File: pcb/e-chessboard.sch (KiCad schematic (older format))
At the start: 46 parts

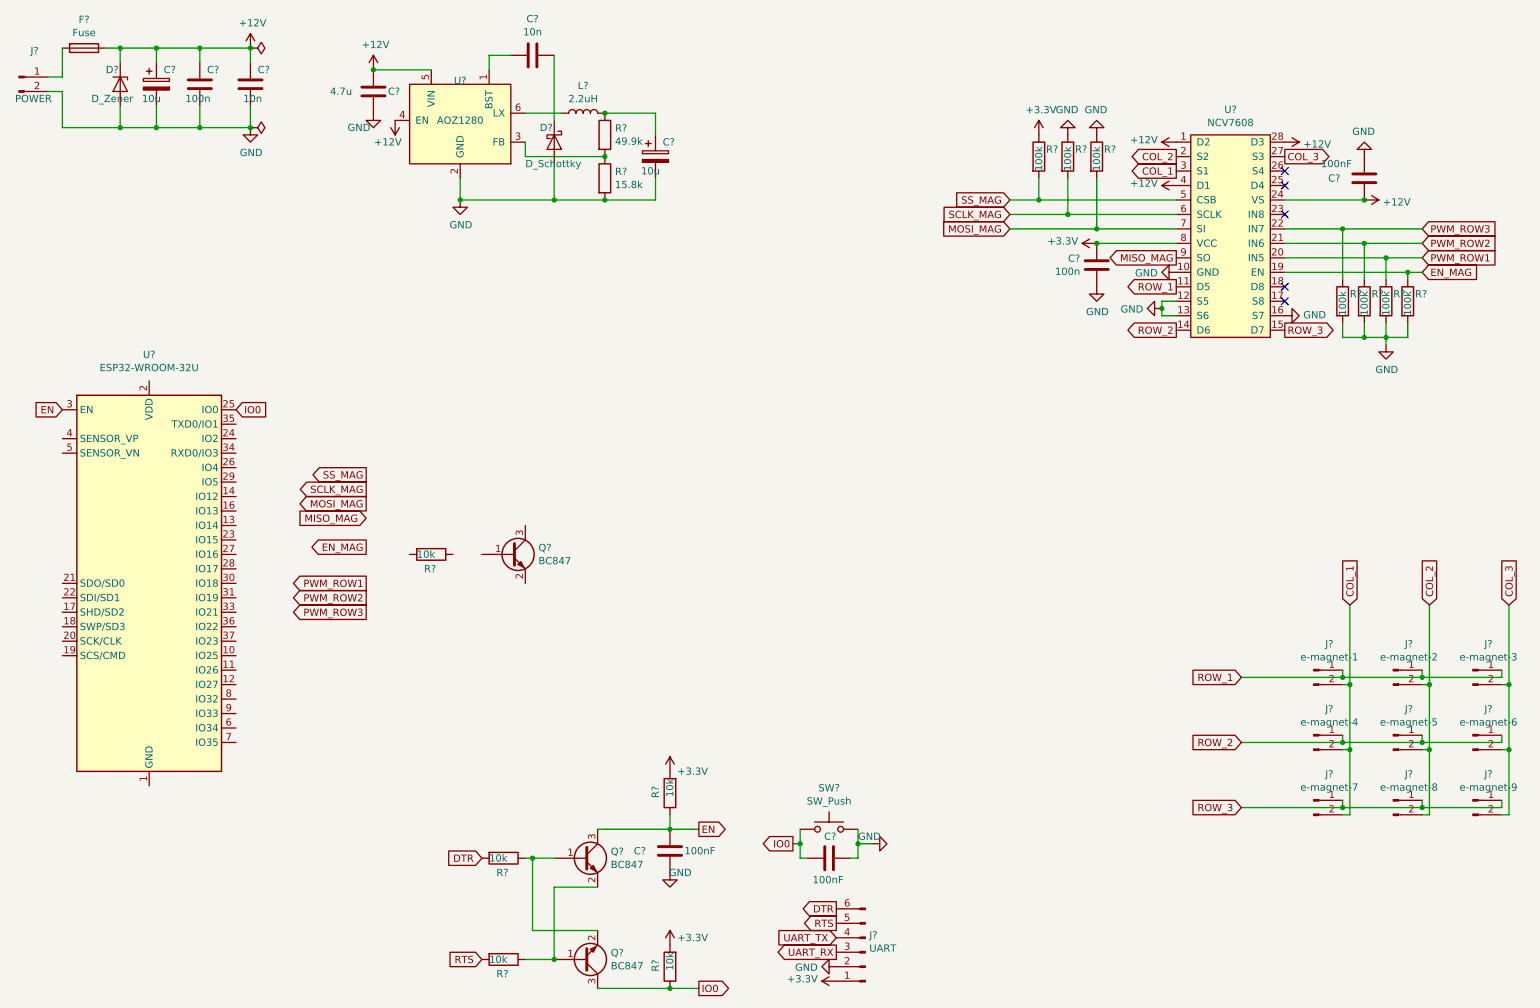
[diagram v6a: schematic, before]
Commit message: feat(kicad): Adding connections to ESP32
Connecting everything together, putting pull-up/downs for spi to the
esp32, powering the esp32.
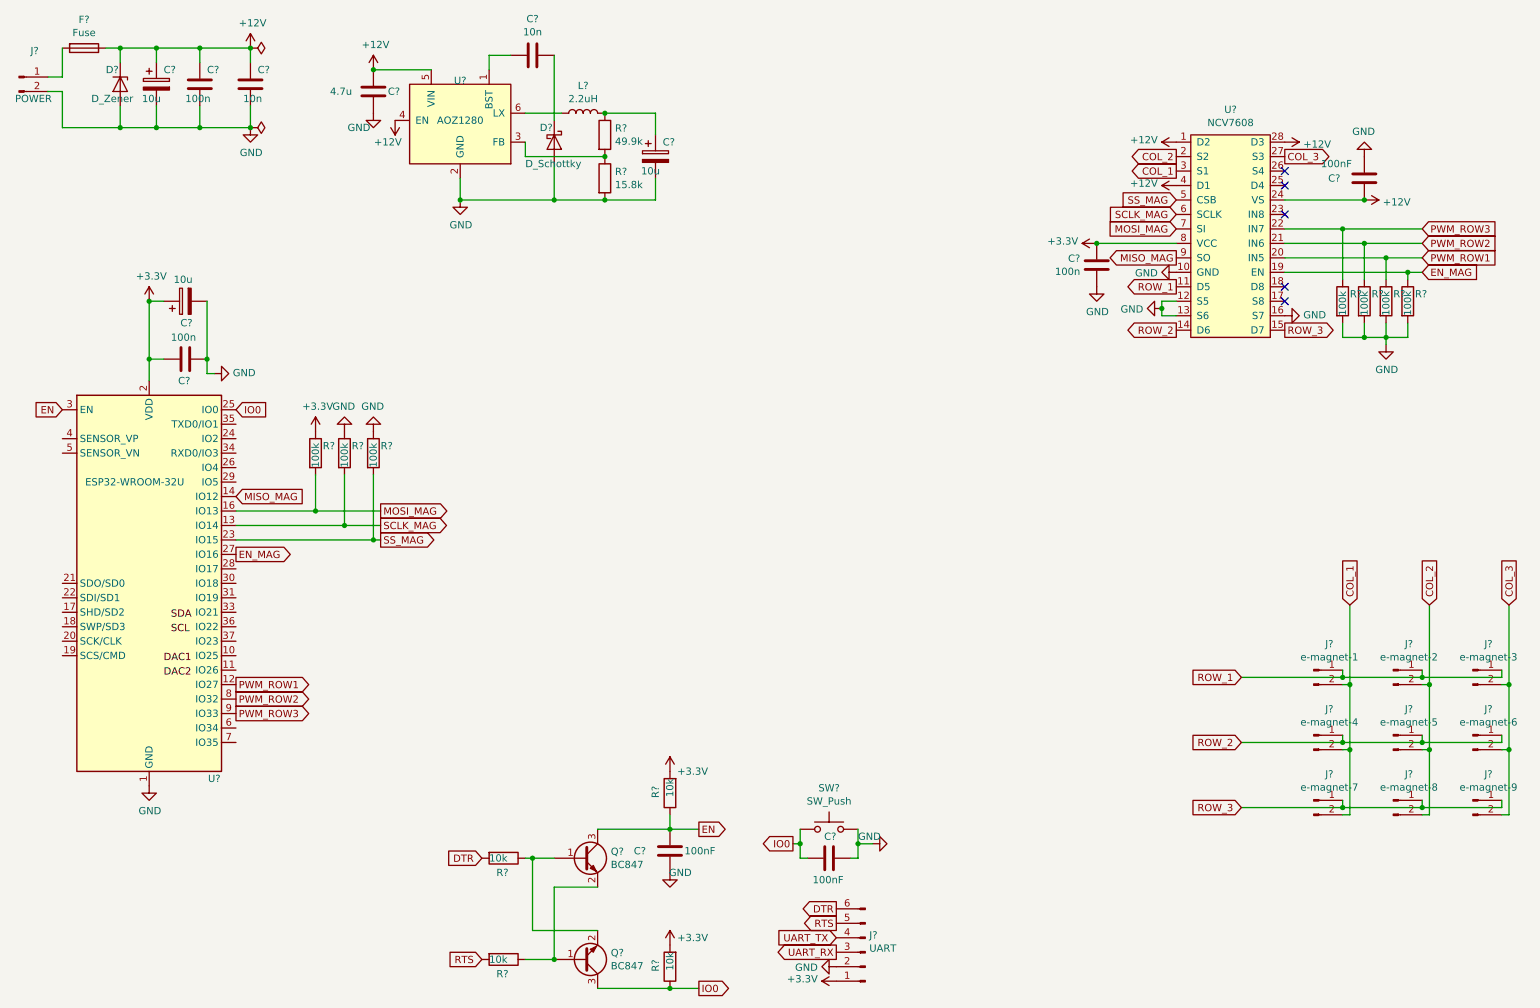
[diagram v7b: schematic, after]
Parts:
- removed Q?: BC847, Package_TO_SOT_SMD:SOT-23, symbol Transistor_BJT:BC847
- removed R?: 10k, Resistor_SMD:R_0805_2012Metric, symbol Device:R
- added C?: 100n, Capacitor_SMD:C_0805_2012Metric_Pad1.15x1.40mm_HandSolder, symbol Device:C
- added C?: 10u, Capacitor_Tantalum_SMD:CP_EIA-3528-21_Kemet-B, symbol Device:CP
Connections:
- net +3V3: now also U?.2 (VDD), C?.1, C?.2
- net EN_MAG: now also U?.27 (IO16)
- net GND: now also U?.1 (GND), U?.15 (GND), U?.38 (GND), U?.39 (GND), C?.1, C?.2
- net MISO_MAG: now also U?.14 (IO12)
- net MOSI_MAG: now also R?.2, U?.16 (IO13); no longer R?.2
- net PWM_ROW1: now also U?.12 (IO27)
- net PWM_ROW2: now also U?.8 (IO32)
- net PWM_ROW3: now also U?.9 (IO33)
- net SCLK_MAG: now also U?.13 (IO14)
- net SS_MAG: now also R?.2, U?.23 (IO15); no longer R?.2
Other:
- moved on the sheet: R?

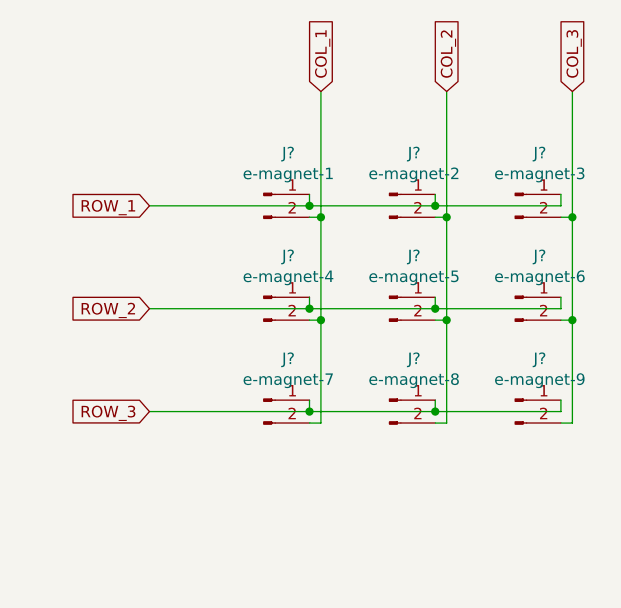
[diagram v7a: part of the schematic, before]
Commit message: fix(kicad): adding diodes to magnets
Adding missing reverse current diodes to the magnets.
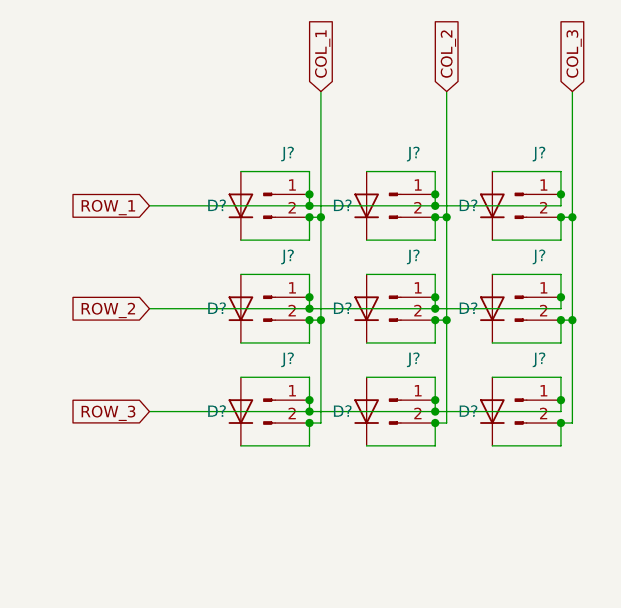
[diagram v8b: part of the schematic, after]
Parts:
- added D? (x9): D, Diode_SMD:D_SMA, symbol Device:D
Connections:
- net COL_1: now also D?.1 (K), D?.1 (K), D?.1 (K)
- net COL_2: now also D?.1 (K), D?.1 (K), D?.1 (K)
- net COL_3: now also D?.1 (K), D?.1 (K), D?.1 (K)
- net ROW_1: now also D?.2 (A), D?.2 (A), D?.2 (A)
- net ROW_2: now also D?.2 (A), D?.2 (A), D?.2 (A)
- net ROW_3: now also D?.2 (A), D?.2 (A), D?.2 (A)
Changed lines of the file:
@@
 P 10000 5200
 F 0 "J?" H 10108 5381 50  0000 C CNN
-F 1 "e-magnet-2" H 10108 5290 50  0000 C CNN
+F 1 "e-magnet-2" H 10108 5290 50  0001 C CNN
 F 2 "lib_fp:20_15_electromagnet" H 10000 5200 50  0001 C CNN
 F 3 "~" H 10000 5200 50  0001 C CNN
@@
 P 10000 5650
 F 0 "J?" H 10108 5831 50  0000 C CNN
-F 1 "e-magnet-5" H 10108 5740 50  0000 C CNN
+F 1 "e-magnet-5" H 10108 5740 50  0001 C CNN
 F 2 "lib_fp:20_15_electromagnet" H 10000 5650 50  0001 C CNN
 F 3 "~" H 10000 5650 50  0001 C CNN
@@
 P 10000 6100
 F 0 "J?" H 10108 6281 50  0000 C CNN
-F 1 "e-magnet-8" H 10108 6190 50  0000 C CNN
+F 1 "e-magnet-8" H 10108 6190 50  0001 C CNN
 F 2 "lib_fp:20_15_electromagnet" H 10000 6100 50  0001 C CNN
 F 3 "~" H 10000 6100 50  0001 C CNN
@@
 P 9450 5650
 F 0 "J?" H 9558 5831 50  0000 C CNN
-F 1 "e-magnet-4" H 9558 5740 50  0000 C CNN
+F 1 "e-magnet-4" H 9558 5740 50  0001 C CNN
 F 2 "lib_fp:20_15_electromagnet" H 9450 5650 50  0001 C CNN
 F 3 "~" H 9450 5650 50  0001 C CNN
@@
 P 9450 5200
 F 0 "J?" H 9558 5381 50  0000 C CNN
-F 1 "e-magnet-1" H 9558 5290 50  0000 C CNN
+F 1 "e-magnet-1" H 9558 5290 50  0001 C CNN
 F 2 "lib_fp:20_15_electromagnet" H 9450 5200 50  0001 C CNN
 F 3 "~" H 9450 5200 50  0001 C CNN
@@
 P 10550 5200
 F 0 "J?" H 10658 5381 50  0000 C CNN
-F 1 "e-magnet-3" H 10658 5290 50  0000 C CNN
+F 1 "e-magnet-3" H 10658 5290 50  0001 C CNN
 F 2 "lib_fp:20_15_electromagnet" H 10550 5200 50  0001 C CNN
 F 3 "~" H 10550 5200 50  0001 C CNN
@@
 P 9450 6100
 F 0 "J?" H 9558 6281 50  0000 C CNN
-F 1 "e-magnet-7" H 9558 6190 50  0000 C CNN
+F 1 "e-magnet-7" H 9558 6190 50  0001 C CNN
 F 2 "lib_fp:20_15_electromagnet" H 9450 6100 50  0001 C CNN
 F 3 "~" H 9450 6100 50  0001 C CNN
@@
 P 10550 5650
 F 0 "J?" H 10658 5831 50  0000 C CNN
-F 1 "e-magnet-6" H 10658 5740 50  0000 C CNN
+F 1 "e-magnet-6" H 10658 5740 50  0001 C CNN
 F 2 "lib_fp:20_15_electromagnet" H 10550 5650 50  0001 C CNN
 F 3 "~" H 10550 5650 50  0001 C CNN
@@
 P 10550 6100
 F 0 "J?" H 10658 6281 50  0000 C CNN
-F 1 "e-magnet-9" H 10658 6190 50  0000 C CNN
+F 1 "e-magnet-9" H 10658 6190 50  0001 C CNN
 F 2 "lib_fp:20_15_electromagnet" H 10550 6100 50  0001 C CNN
 F 3 "~" H 10550 6100 50  0001 C CNN
@@
 Wire Wire Line
 	10200 5250 10200 5200
-Connection ~ 10200 5250
 Wire Wire Line
 	9650 5250 9650 5200
@@
 Wire Wire Line
 	9650 5700 10200 5700
-Wire Wire Line
-	9650 5250 10200 5250
 Wire Wire Line
 	10200 6150 10750 6150
@@
 Text Label 1500 5250 0    50   ~ 0
 DAC2
+$Comp
+L Device:D D?
+U 1 1 5EA27C27
+P 9900 5250
+F 0 "D?" V 9900 5400 50  0000 R CNN
+F 1 "D" V 9945 5329 50  0001 L CNN
+F 2 "Diode_SMD:D_SMA" H 9900 5250 50  0001 C CNN
+F 3 "http://www.smc-diodes.com/propdf/S1A-S1M%20N0560%20REV.B.pdf" H 9900 5250 50  0001 C CNN
+	1    9900 5250
+	0    -1   -1   0
+$EndComp
+Wire Wire Line
+	9650 5250 10200 5250
+Connection ~ 10200 5250
+$Comp
+L Device:D D?
+U 1 1 5EA43EF8
+P 10450 5250
+F 0 "D?" V 10450 5400 50  0000 R CNN
+F 1 "D" V 10495 5329 50  0001 L CNN
+F 2 "Diode_SMD:D_SMA" H 10450 5250 50  0001 C CNN
+F 3 "http://www.smc-diodes.com/propdf/S1A-S1M%20N0560%20REV.B.pdf" H 10450 5250 50  0001 C CNN
+	1    10450 5250
+	0    -1   -1   0
+$EndComp
+$Comp
+L Device:D D?
+U 1 1 5EA44385
+P 10450 5700
+F 0 "D?" V 10450 5850 50  0000 R CNN
+F 1 "D" V 10495 5779 50  0001 L CNN
+F 2 "Diode_SMD:D_SMA" H 10450 5700 50  0001 C CNN
+F 3 "http://www.smc-diodes.com/propdf/S1A-S1M%20N0560%20REV.B.pdf" H 10450 5700 50  0001 C CNN
+	1    10450 5700
+	0    -1   -1   0
+$EndComp
+$Comp
+L Device:D D?
+U 1 1 5EA44F68
+P 9900 5700
+F 0 "D?" V 9900 5850 50  0000 R CNN
+F 1 "D" V 9945 5779 50  0001 L CNN
+F 2 "Diode_SMD:D_SMA" H 9900 5700 50  0001 C CNN
+F 3 "http://www.smc-diodes.com/propdf/S1A-S1M%20N0560%20REV.B.pdf" H 9900 5700 50  0001 C CNN
+	1    9900 5700
+	0    -1   -1   0
+$EndComp
+$Comp
+L Device:D D?
+U 1 1 5EA4556E
+P 9350 5700
+F 0 "D?" V 9350 5850 50  0000 R CNN
+F 1 "D" V 9395 5779 50  0001 L CNN
+F 2 "Diode_SMD:D_SMA" H 9350 5700 50  0001 C CNN
+F 3 "http://www.smc-diodes.com/propdf/S1A-S1M%20N0560%20REV.B.pdf" H 9350 5700 50  0001 C CNN
+	1    9350 5700
+	0    -1   -1   0
+$EndComp
+$Comp
+L Device:D D?
+U 1 1 5EA45981
+P 9350 6150
+F 0 "D?" V 9350 6300 50  0000 R CNN
+F 1 "D" V 9395 6229 50  0001 L CNN
+F 2 "Diode_SMD:D_SMA" H 9350 6150 50  0001 C CNN
+F 3 "http://www.smc-diodes.com/propdf/S1A-S1M%20N0560%20REV.B.pdf" H 9350 6150 50  0001 C CNN
+	1    9350 6150
+	0    -1   -1   0
+$EndComp
+$Comp
+L Device:D D?
+U 1 1 5EA45E30
+P 9900 6150
+F 0 "D?" V 9900 6300 50  0000 R CNN
+F 1 "D" V 9945 6229 50  0001 L CNN
+F 2 "Diode_SMD:D_SMA" H 9900 6150 50  0001 C CNN
+F 3 "http://www.smc-diodes.com/propdf/S1A-S1M%20N0560%20REV.B.pdf" H 9900 6150 50  0001 C CNN
+	1    9900 6150
+	0    -1   -1   0
+$EndComp
+$Comp
+L Device:D D?
+U 1 1 5EA462B8
+P 10450 6150
+F 0 "D?" V 10450 6300 50  0000 R CNN
+F 1 "D" V 10495 6229 50  0001 L CNN
+F 2 "Diode_SMD:D_SMA" H 10450 6150 50  0001 C CNN
+F 3 "http://www.smc-diodes.com/propdf/S1A-S1M%20N0560%20REV.B.pdf" H 10450 6150 50  0001 C CNN
+	1    10450 6150
+	0    -1   -1   0
+$EndComp
+Wire Wire Line
+	9350 5400 9650 5400
+Wire Wire Line
+	9650 5400 9650 5300
+Connection ~ 9650 5300
+Wire Wire Line
+	9900 5100 10200 5100
+Wire Wire Line
+	10200 5100 10200 5200
+Connection ~ 10200 5200
+Wire Wire Line
+	10200 5300 10200 5400
+Wire Wire Line
+	10200 5400 9900 5400
+Connection ~ 10200 5300
+Wire Wire Line
+	10450 5400 10750 5400
+Wire Wire Line
+	10750 5400 10750 5300
+Connection ~ 10750 5300
+Wire Wire Line
+	10750 5200 10750 5100
+Wire Wire Line
+	10750 5100 10450 5100
+Connection ~ 10750 5200
+Wire Wire Line
+	10450 5550 10750 5550
+Wire Wire Line
+	10750 5550 10750 5650
+Connection ~ 10750 5650
+Wire Wire Line
+	10750 5750 10750 5850
+Wire Wire Line
+	10750 5850 10450 5850
+Connection ~ 10750 5750
+Wire Wire Line
+	10200 5850 10200 5750
+Wire Wire Line
+	9900 5850 10200 5850
+Connection ~ 10200 5750
+Wire Wire Line
+	10200 5650 10200 5550
+Wire Wire Line
+	10200 5550 9900 5550
+Connection ~ 10200 5650
+Wire Wire Line
+	9350 5850 9650 5850
+Wire Wire Line
+	9650 5850 9650 5750
+Connection ~ 9650 5750
+Wire Wire Line
+	9650 5650 9650 5550
+Wire Wire Line
+	9650 5550 9350 5550
+Connection ~ 9650 5650
+Wire Wire Line
+	9350 6000 9650 6000
+Wire Wire Line
+	9650 6000 9650 6100
+Connection ~ 9650 6100
+Wire Wire Line
+	9350 6300 9650 6300
+Wire Wire Line
+	9650 6300 9650 6200
+Connection ~ 9650 6200
+Wire Wire Line
+	9900 6300 10200 6300
+Wire Wire Line
+	10200 6300 10200 6200
+Connection ~ 10200 6200
+Wire Wire Line
+	10200 6100 10200 6000
+Wire Wire Line
+	10200 6000 9900 6000
+Connection ~ 10200 6100
+Wire Wire Line
+	10450 6000 10750 6000
+Wire Wire Line
+	10750 6000 10750 6100
+Connection ~ 10750 6100
+Wire Wire Line
+	10750 6200 10750 6300
+Wire Wire Line
+	10750 6300 10450 6300
+Connection ~ 10750 6200
+$Comp
+L Device:D D?
+U 1 1 5EA0FF58
+P 9350 5250
+F 0 "D?" V 9350 5400 50  0000 R CNN
+F 1 "D" V 9395 5329 50  0001 L CNN
+F 2 "Diode_SMD:D_SMA" H 9350 5250 50  0001 C CNN
+F 3 "http://www.smc-diodes.com/propdf/S1A-S1M%20N0560%20REV.B.pdf" H 9350 5250 50  0001 C CNN
+	1    9350 5250
+	0    -1   -1   0
+$EndComp
+Wire Wire Line
+	9350 5100 9650 5100
+Wire Wire Line
+	9650 5100 9650 5200
+Connection ~ 9650 5200
 $EndSCHEMATC
